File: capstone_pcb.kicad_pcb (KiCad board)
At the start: 4 copper layers, 60.2 x 43.6 mm, 48 parts, among them IC6 BSS138, J1 Conn_01x05, Q1 BSS138, U1 TPS610994DRV, U2 BMI270, U3 NRF52840-QIAA-R, U4 MAX30102EFD+T, U5 AMS1117-1.8, X1 32MHz, X2 32.768kHz

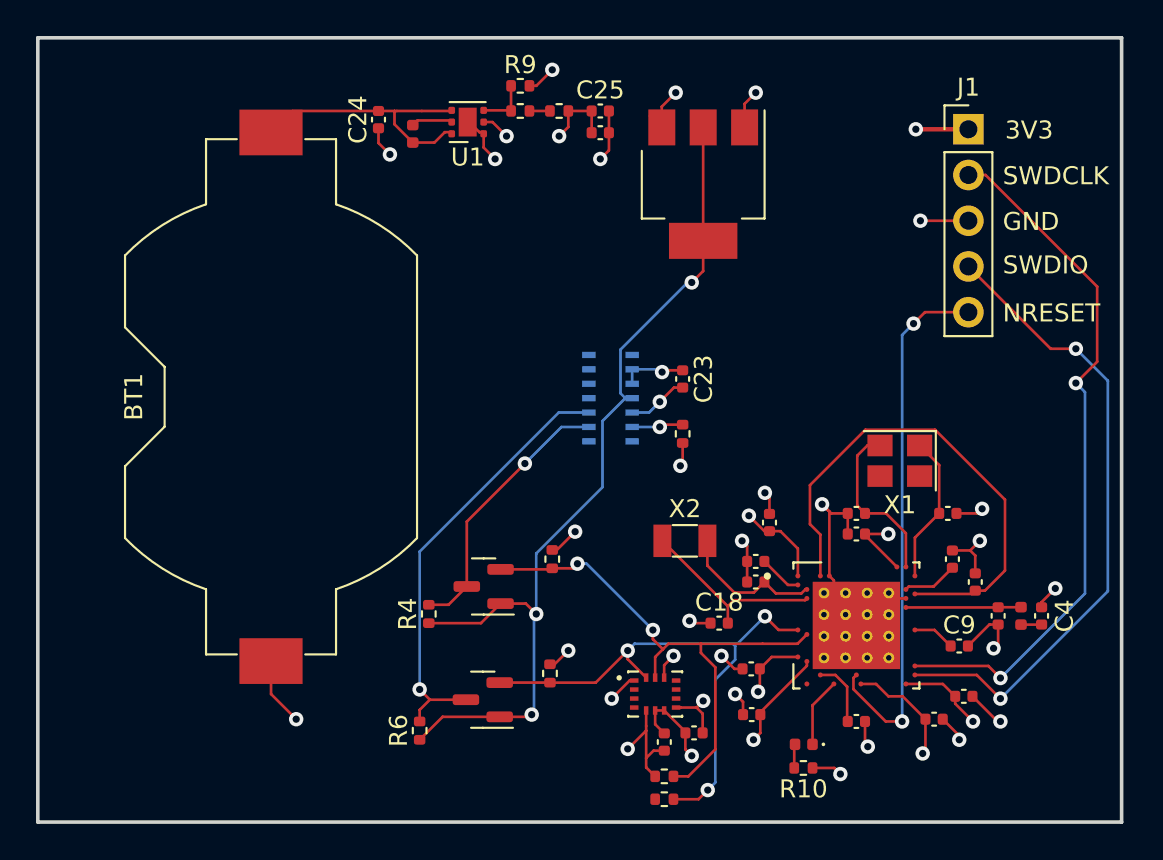
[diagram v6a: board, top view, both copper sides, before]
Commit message: edit nrf pads and properties
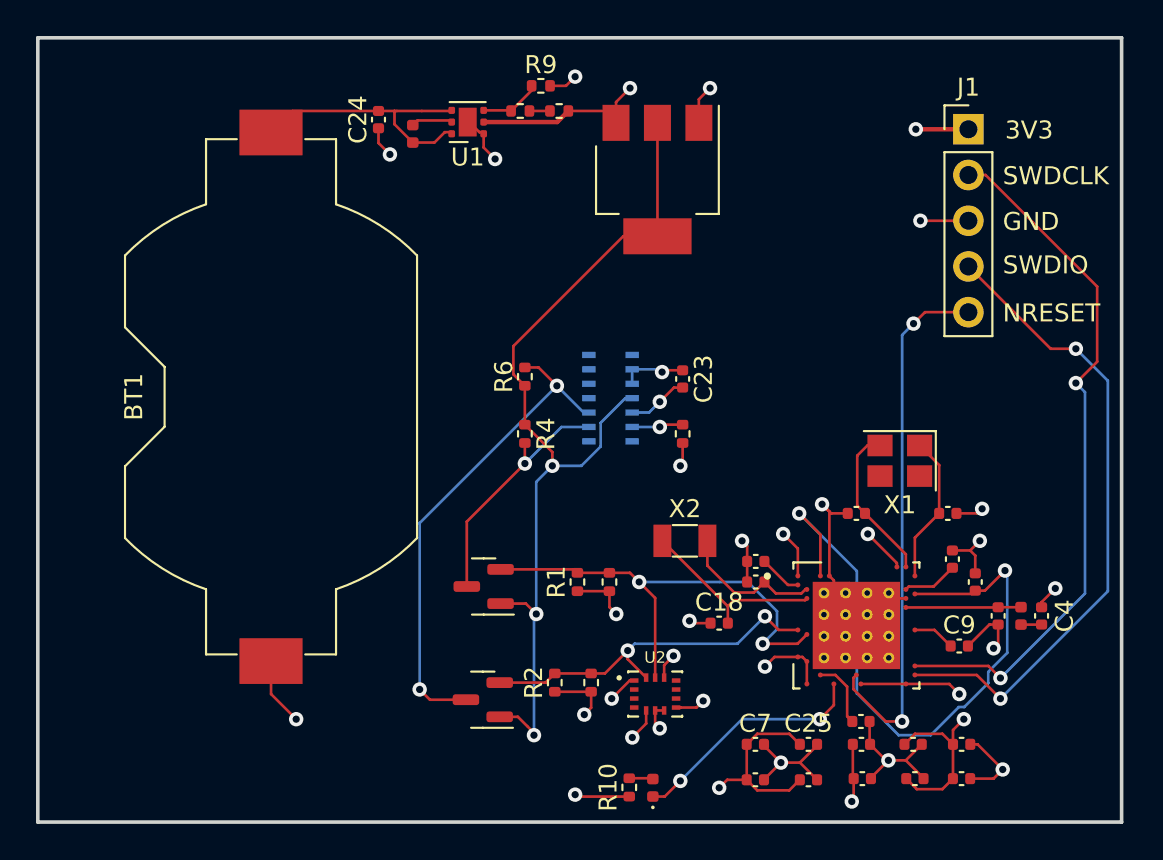
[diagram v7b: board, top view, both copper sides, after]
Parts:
- moved C26 37.8 mm to (123.2, 86.9)
- moved C25 37.0 mm to (123.2, 85.0)
- moved R6 20.5 mm to (107.4, 64.5)
- moved C14 16.4 mm to (129.1, 86.9), turned to 0 degrees
- moved C16 15.1 mm to (131.7, 86.9), turned to 0 degrees
- moved C21 13.8 mm to (129.0, 85.0), turned to 0 degrees
- moved C8 12.5 mm to (120.2, 86.9)
- moved R1 11.8 mm to (110.4, 75.9), turned to 90 degrees
- moved C19 11.8 mm to (131.7, 85.0), turned to 0 degrees
- moved C12 11.7 mm to (126.1, 85.0), turned to 0 degrees
- moved R4 11.3 mm to (107.4, 67.7), turned to -90 degrees
- moved C7 10.0 mm to (120.2, 85.0)
- moved R10 9.73 mm to (113.2, 87.4), turned to 90 degrees
- moved R2 8.89 mm to (109.1, 81.5), turned to 90 degrees
- moved D1 8.72 mm to (114.6, 87.4), turned to 90 degrees
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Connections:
- U3 pad 74_1: (no net) -> GND
- U3 pad 74_10: (no net) -> GND
- U3 pad 74_11: (no net) -> GND
- U3 pad 74_12: (no net) -> GND
- U3 pad 74_13: (no net) -> GND
- U3 pad 74_14: (no net) -> GND
- U3 pad 74_15: (no net) -> GND
- U3 pad 74_16: (no net) -> GND
- U3 pad 74_2: (no net) -> GND
- U3 pad 74_3: (no net) -> GND
- U3 pad 74_4: (no net) -> GND
- U3 pad 74_5: (no net) -> GND
- U3 pad 74_6: (no net) -> GND
- U3 pad 74_7: (no net) -> GND
- U3 pad 74_8: (no net) -> GND
- U3 pad 74_9: (no net) -> GND
- U3 pad AD2: /AD2 -> +3V3
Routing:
- net /SDA: track 31.5 -> 20.3 mm, vias 3 -> 2
- net Net-(D1-K): track 3.85 -> 13.3 mm, vias 0 -> 2
- net +3V3: track 58.8 -> 67.9 mm, vias 17 -> 16
- net /DEC4 6: track 28.5 -> 37.0 mm, vias 0 -> 2
- net /SCL: track 30.6 -> 26.8 mm
- net /BSDA: track 24.5 -> 27.4 mm, vias 1 -> 2
- net GND: track 70.1 -> 72.0 mm, vias 23 -> 19
- net /BSCL: track 15.3 -> 13.9 mm
- net Net-(U3-XC2): track 9.48 -> 8.80 mm

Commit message: replaced nrf 3.3v w/ 3v, added 3v power plane
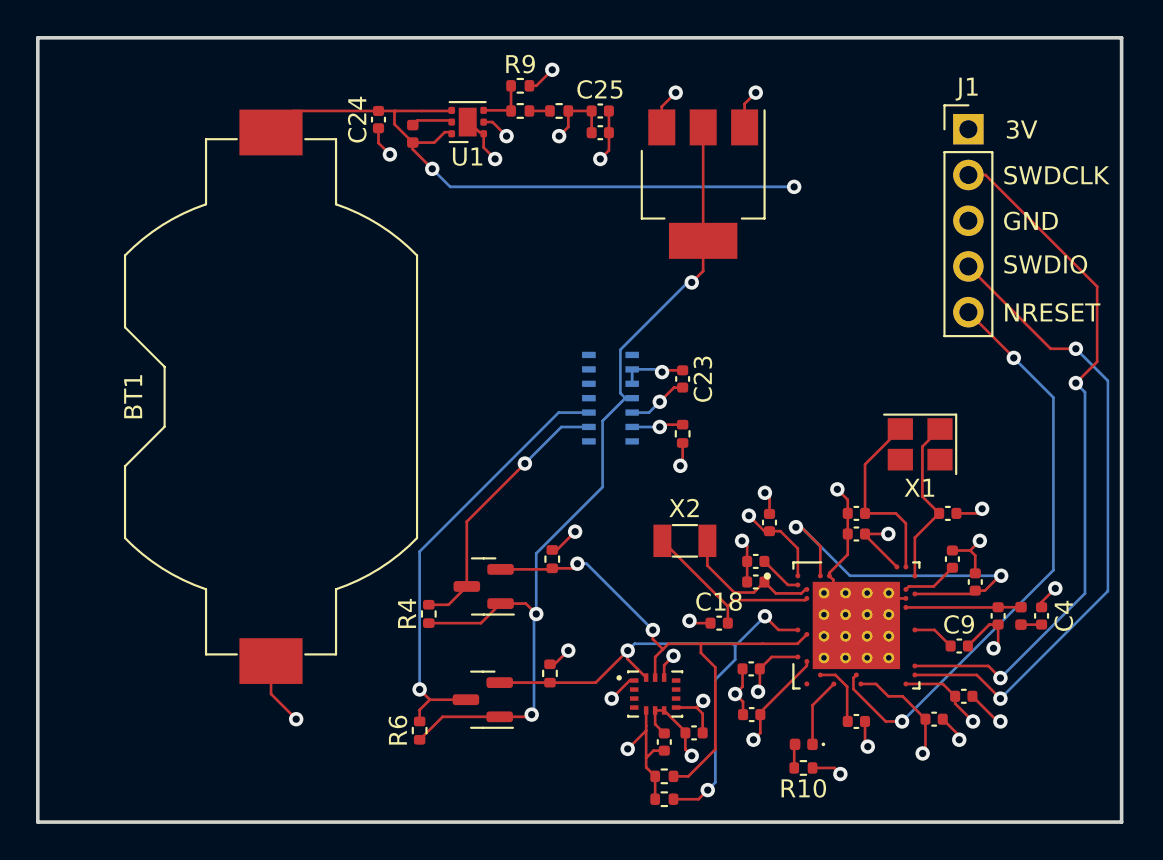
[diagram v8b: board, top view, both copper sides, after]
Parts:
- moved C26 37.8 mm to (111.6, 51.0)
- moved C25 37.0 mm to (111.6, 49.8)
- moved R6 20.5 mm to (101.6, 84.2)
- moved C14 16.4 mm to (121.0, 72.6), turned to 90 degrees
- moved C16 15.1 mm to (116.8, 84.3), turned to 180 degrees
- moved C21 13.8 mm to (115.2, 84.8), turned to 90 degrees
- moved C8 12.5 mm to (131.8, 82.3)
- moved R1 11.8 mm to (115.2, 86.7), turned to 0 degrees
- moved C19 11.8 mm to (120.0, 83.3), turned to 180 degrees
- moved C12 11.7 mm to (125.9, 73.3), turned to 180 degrees
- moved R4 11.3 mm to (102.1, 77.7), turned to 90 degrees
- moved C7 10.0 mm to (130.2, 83.6)
- moved R10 9.73 mm to (122.9, 86.3), turned to 180 degrees
- moved R2 8.89 mm to (115.2, 88.0), turned to 0 degrees
- moved D1 8.72 mm to (122.9, 85.0), turned to 180 degrees
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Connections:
- C12 pad 1: +3V3 -> +3V
- C14 pad 1: +3V3 -> +3V
- C19 pad 1: +3V3 -> +3V
- C6 pad 1: +3V3 -> +3V
- C7 pad 1: +3V3 -> +3V
- C8 pad 1: +3V3 -> +3V
- J1 pad 1: +3V3 -> +3V
- R10 pad 1: +3V3 -> +3V
- U3 pad 74_1: GND -> (no net)
- U3 pad 74_10: GND -> (no net)
- U3 pad 74_11: GND -> (no net)
- U3 pad 74_12: GND -> (no net)
- U3 pad 74_13: GND -> (no net)
- U3 pad 74_14: GND -> (no net)
- U3 pad 74_15: GND -> (no net)
- U3 pad 74_16: GND -> (no net)
- U3 pad 74_2: GND -> (no net)
- U3 pad 74_3: GND -> (no net)
- U3 pad 74_4: GND -> (no net)
- U3 pad 74_5: GND -> (no net)
- U3 pad 74_6: GND -> (no net)
- U3 pad 74_7: GND -> (no net)
- U3 pad 74_8: GND -> (no net)
- U3 pad 74_9: GND -> (no net)
- U3 pad A22: +3V3 -> +3V
- U3 pad AD14: +3V3 -> +3V
- U3 pad AD2: +3V3 -> unconnected-(U3-VBUS-PadAD2)
- U3 pad AD23: +3V3 -> +3V
- U3 pad B1: +3V3 -> +3V
- U3 pad W1: +3V3 -> +3V
- U3 pad Y2: +3V3 -> +3V
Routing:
- net +3V: track 15.2 -> 68.6 mm, vias 0 -> 9
- net +3V3: track 67.9 -> 26.2 mm, vias 16 -> 9
- net /DEC4 6: track 37.0 -> 21.2 mm
- net GND: track 72.0 -> 60.6 mm, vias 19 -> 21
- net /SDA: track 20.3 -> 31.5 mm, vias 2 -> 3
- net Net-(D1-K): track 13.3 -> 3.85 mm, vias 2 -> 0
- net /SCL: track 26.8 -> 30.6 mm
- net /BSDA: track 27.4 -> 24.5 mm, vias 2 -> 1
- net Net-(J1-Pin_5): track 30.0 -> 32.5 mm
- net Net-(U3-XC2): track 8.80 -> 10.4 mm
- net /BSCL: track 13.9 -> 15.3 mm
- net Net-(U3-XC1): track 8.25 -> 9.51 mm
- added copper zone on In2.Cu, net +3V
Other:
- board text added: "3V"
- board text removed: "3V3"
